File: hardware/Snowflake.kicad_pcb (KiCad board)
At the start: 2 copper layers, 70.5 x 79.8 mm, 40 parts, among them Q1 Q_DUAL_NMOS, SW1 SW_SPST, U1 Opamp_Single_MCP6001, U2 TL431D, U3 74HC595

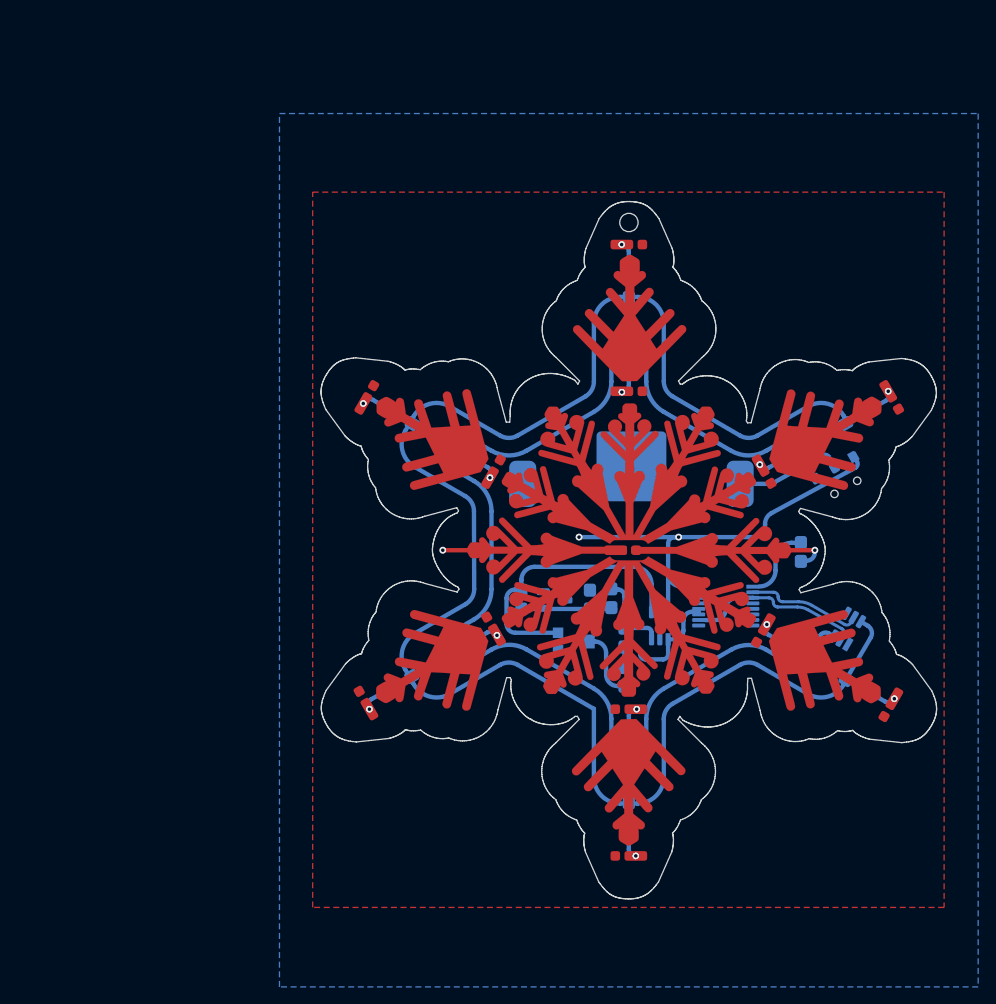
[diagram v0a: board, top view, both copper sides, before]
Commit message: Pre-test push. Happy with the layout, waiting for the tests to choose an LED, resitor and battery holder
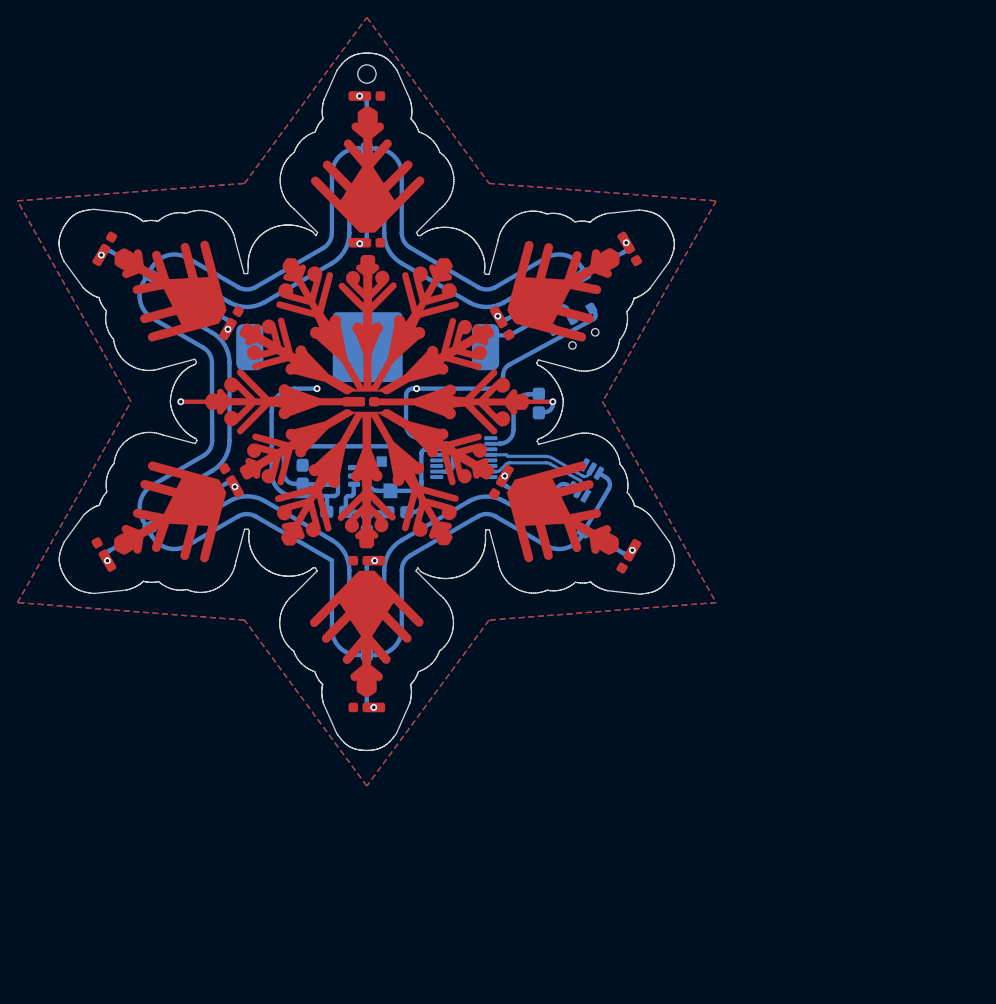
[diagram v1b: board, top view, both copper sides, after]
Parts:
- removed the R2 at (129.5, 131.5)
- removed R4: R_Small, Snowflake:0805-R_Handsolder
- removed U3: 74HC595, Snowflake:16-TSSOP_5x6.5mm_P0.65-74HC565
- added R1: 10k, Snowflake:0805-R_Handsolder, B.Cu at (96.5, 112.6)
- added REF**: Turn_This!, Snowflake:Turn_This!, B.Cu at (106.5, 115.8)
- BT1: footprint Snowflake:CR2032_Multicomp_MP000357_Alternative -> Snowflake:CR2032_X2_Keystone_3074_
- C1: value C_Small -> C
- Q1: value Q_DUAL_NMOS -> NX3008NBKS
- R2: renamed from R1; value R_Small -> 10k
- R5: renamed from R3; value R_Small -> 10k
- RV1: value R_POT_Small -> 0-50k
- U1: value Opamp_Single_MCP6001 -> MCP6001
- U2: value TL431D -> CD74HC4017; footprint Snowflake:SOT-23_LM4041_1.2V_Handsolder -> Snowflake:16-TSSOP_5x6.5mm_P0.65-CD54HC4017
- moved U1 40.4 mm to (97.0, 108.5), turned to -90 degrees
- moved D1 34.5 mm to (99.3, 100.0)
- moved R12 34.5 mm to (125.8, 115.3)
- moved D10 34.5 mm to (84.5, 109.0)
- moved D11 34.5 mm to (69.9, 117.5)
- moved D12 34.5 mm to (84.5, 91.0)
- moved D13 34.5 mm to (70.0, 82.5)
- moved D2 34.5 mm to (100.0, 81.8)
- moved D3 34.5 mm to (100.0, 65.0)
- moved D4 34.5 mm to (115.5, 91.0)
- moved D5 34.5 mm to (130.1, 82.5)
- moved D6 34.5 mm to (115.4, 109.2)
- moved D9 34.5 mm to (100.0, 135.0)
- moved Logo1 34.5 mm to (100.0, 100.0)
- moved Q1 34.5 mm to (125.0, 109.0)
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- renumbered R9 to R10, R10 to R11, R11 to R12, R12 to R13, R13 to R14, R14 to R15, R15 to R16, R16 to R17, R17 to R18, R5 to R6, R6 to R7, R7 to R8, R8 to R9
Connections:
- C1 pad 2: VBIAS -> GND
- R5 pad 2: Net-(R3-Pad2) -> VBIAS
- RV1 pad 2: Net-(R2-Pad2) -> CLK
- SW1 pad 3: (no net) -> unconnected-(SW1-Pad3)
- U1 pad 3: Net-(R3-Pad2) -> VBIAS
- U2 pad 1: VBIAS -> unconnected-(U2-Pad1)
- U2 pad 2: GND -> LED0
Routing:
- net VBAT: track 49.8 -> 62.4 mm
- net Net-(C1-Pad1): track 32.5 -> 22.6 mm
- net Net-(R3-Pad2): track 9.78 -> 0.00 mm
- net Net-(R2-Pad2): track 8.34 -> 0.00 mm
- net DRIVE_ROW1: track 20.5 -> 12.6 mm
- net RESET: track 0.00 -> 6.21 mm
- net CLK: track 16.6 -> 19.9 mm
- net VBIAS: track 10.8 -> 8.69 mm
- net ROW0: track 152.8 -> 151.7 mm
- net ROW1: track 196.5 -> 195.6 mm
- net LED0: track 8.74 -> 9.56 mm
- net DRIVE_ROW0: track 13.3 -> 12.6 mm

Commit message: Happy with the HW
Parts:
- added R5: 10k, Snowflake:0805-R_Handsolder_NoSilk, B.Cu at (89.7, 105.1)
- added R6: 10k, Snowflake:0805-R_Handsolder_NoSilk, B.Cu at (89.7, 107.2)
- BT1: footprint Snowflake:CR2032_X2_Keystone_3074_ -> Snowflake:CR2032_X2_Keystone_3074_NoSilk
- C1: value C -> 4.7μ; footprint Snowflake:0805-C_Handsolder -> Snowflake:0805-C_Handsolder_NoSilk
- Q1: footprint Snowflake:SOT-23-6_DMN2004DMK_Handsoldering -> Snowflake:SOT-23-6_DMN2004DMK_Handsoldering_NoSilk
- R1, R2: footprint Snowflake:0805-R_Handsolder -> Snowflake:0805-R_Handsolder_NoSilk
- R10: renamed from R8; footprint Snowflake:0805-R_Handsolder -> Snowflake:0805-R_Handsolder_NoSilk
- R11: renamed from R9; footprint Snowflake:0805-R_Handsolder -> Snowflake:0805-R_Handsolder_NoSilk
- R12: renamed from R10; footprint Snowflake:0805-R_Handsolder -> Snowflake:0805-R_Handsolder_NoSilk
- R13: renamed from R11; footprint Snowflake:0805-R_Handsolder -> Snowflake:0805-R_Handsolder_NoSilk
- R14: renamed from R12; footprint Snowflake:0805-R_Handsolder -> Snowflake:0805-R_Handsolder_NoSilk
- R15: renamed from R13; footprint Snowflake:0805-R_Handsolder -> Snowflake:0805-R_Handsolder_NoSilk
- R16: renamed from R14; footprint Snowflake:0805-R_Handsolder -> Snowflake:0805-R_Handsolder_NoSilk
- R17: renamed from R15; footprint Snowflake:0805-R_Handsolder -> Snowflake:0805-R_Handsolder_NoSilk
- R18: renamed from R16; footprint Snowflake:0805-R_Handsolder -> Snowflake:0805-R_Handsolder_NoSilk
- R19: renamed from R17; footprint Snowflake:0805-R_Handsolder -> Snowflake:0805-R_Handsolder_NoSilk
- R20: renamed from R18; footprint Snowflake:0805-R_Handsolder -> Snowflake:0805-R_Handsolder_NoSilk
- R7: renamed from R5; footprint Snowflake:0805-R_Handsolder -> Snowflake:0805-R_Handsolder_NoSilk
- R8: renamed from R6; footprint Snowflake:0805-R_Handsolder -> Snowflake:0805-R_Handsolder_NoSilk
- R9: renamed from R7; footprint Snowflake:0805-R_Handsolder -> Snowflake:0805-R_Handsolder_NoSilk
- RV1: footprint Snowflake:Potentiometer_TC33X-2-204E -> Snowflake:Potentiometer_TC33X-2-204E_NoSilk
- SW1: footprint Snowflake:Slider_Switch_C&K_AYZ0102AGRLC_SPDT_RightAngle -> Snowflake:Slider_Switch_C&K_AYZ0102AGRLC_SPDT_RightAngle_NoSilk
- U1: footprint Snowflake:Op_Amp_SOT23_MCP6001T -> Snowflake:Op_Amp_SOT23_MCP6001T_NoSilk
- U2: footprint Snowflake:16-TSSOP_5x6.5mm_P0.65-CD54HC4017 -> Snowflake:16-TSSOP_5x6.5mm_P0.65-CD54HC4017_NoSilk
- moved C1 0.45 mm to (93.1, 108.3)
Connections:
- RV1 pad 3: Net-(C1-Pad1) -> Net-(R5-Pad2)
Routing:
- net Net-(R5-Pad2): track 0.00 -> 16.4 mm
- net Net-(C1-Pad1): track 22.6 -> 10.6 mm
- net VBAT: track 62.4 -> 64.1 mm
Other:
- board text added: "Intentionally left empty"

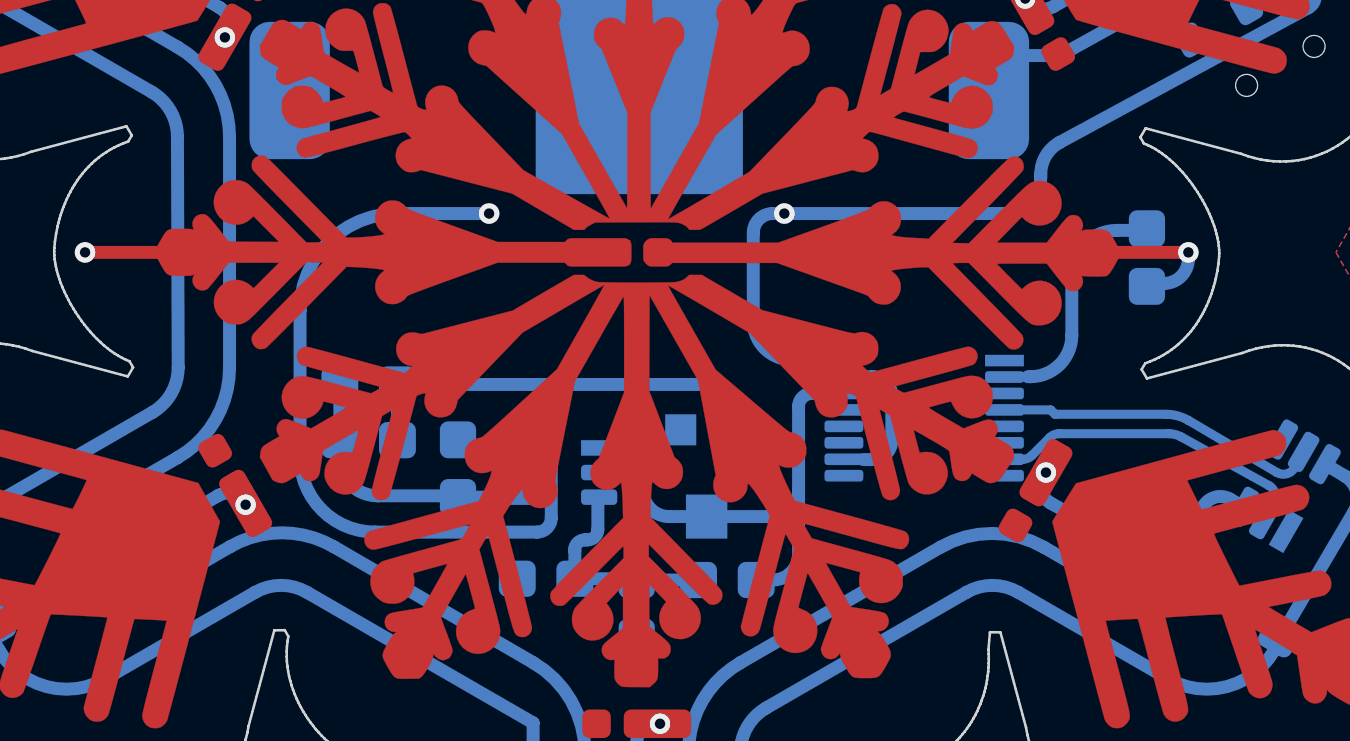
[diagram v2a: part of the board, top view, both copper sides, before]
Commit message: Added Voila and requirements.txt
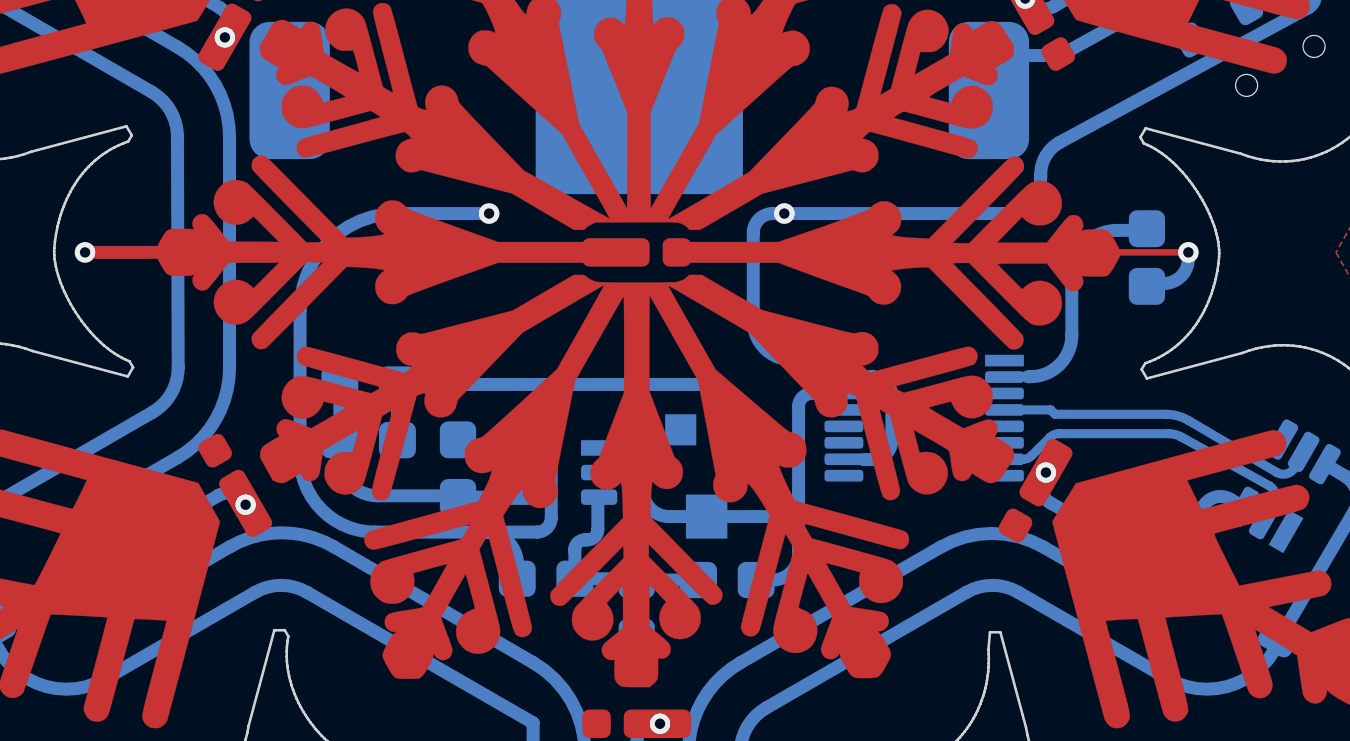
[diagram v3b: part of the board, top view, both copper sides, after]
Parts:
- moved D1 0.70 mm to (100.0, 100.0)
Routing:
- net VBAT: track 64.1 -> 66.6 mm
- net V1: track 22.8 -> 21.6 mm
